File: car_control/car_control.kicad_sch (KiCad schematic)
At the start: 21 parts, among them J1 Conn_01x02, J2 Conn_01x03, J3 Conn_01x03, Q1 IRF540N, Q2 Q_Photo_NPN, SW1 SW_SPST

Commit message: initial schematic done?
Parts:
- added H1, H2, H3, H4: MountingHole, MountingHole:MountingHole_2.7mm_M2.5_DIN965_Pad, symbol Mechanical:MountingHole
- SW1: footprint Connector_PinHeader_2.54mm:PinHeader_1x02_P2.54mm_Vertical -> mini_slide_switch:OS102011MA1QN1; CatNo (none) -> CKN9559-ND
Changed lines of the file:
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@@
+    )
+  )
+  (symbol (lib_id "Mechanical:MountingHole") (at 44.45 129.54 0) (unit 1)
+    (in_bom yes) (on_board yes) (dnp no) (fields_autoplaced)
+    (property "Reference" "H1" (at 46.99 128.905 0)
+      (effects (font (size 1.27 1.27)) (justify left))
+    )
+    (property "Value" "MountingHole" (at 46.99 131.445 0)
+      (effects (font (size 1.27 1.27)) (justify left))
+    )
+    (property "Footprint" "MountingHole:MountingHole_2.7mm_M2.5_DIN965_Pad" (at 44.45 129.54 0)
+      (effects (font (size 1.27 1.27)) hide)
+    )
+    (property "Datasheet" "~" (at 44.45 129.54 0)
+      (effects (font (size 1.27 1.27)) hide)
+    )
+    (instances
+      (project "car_control"
+        (path "/08ff0388-b5fa-44e5-b165-5596a9674913"
+          (reference "H1") (unit 1)
+        )
+      )
     )
   )
@@
     )
   )
+  (symbol (lib_id "Mechanical:MountingHole") (at 44.45 148.59 0) (unit 1)
+    (in_bom yes) (on_board yes) (dnp no) (fields_autoplaced)
+    (property "Reference" "H4" (at 46.99 147.955 0)
+      (effects (font (size 1.27 1.27)) (justify left))
+    )
+    (property "Value" "MountingHole" (at 46.99 150.495 0)
+      (effects (font (size 1.27 1.27)) (justify left))
+    )
+    (property "Footprint" "MountingHole:MountingHole_2.7mm_M2.5_DIN965_Pad" (at 44.45 148.59 0)
+      (effects (font (size 1.27 1.27)) hide)
+    )
+    (property "Datasheet" "~" (at 44.45 148.59 0)
+      (effects (font (size 1.27 1.27)) hide)
+    )
+    (instances
+      (project "car_control"
+        (path "/08ff0388-b5fa-44e5-b165-5596a9674913"
+          (reference "H4") (unit 1)
+        )
+      )
+    )
+  )
   (symbol (lib_id "Device:LED") (at 144.78 113.03 180) (unit 1)
     (in_bom yes) (on_board yes) (dnp no)
@@
         (path "/08ff0388-b5fa-44e5-b165-5596a9674913"
           (reference "BT1") (unit 1)
+        )
+      )
+    )
+  )
+  (symbol (lib_id "Mechanical:MountingHole") (at 44.45 135.89 0) (unit 1)
+    (in_bom yes) (on_board yes) (dnp no) (fields_autoplaced)
+    (property "Reference" "H2" (at 46.99 135.255 0)
+      (effects (font (size 1.27 1.27)) (justify left))
+    )
+    (property "Value" "MountingHole" (at 46.99 137.795 0)
+      (effects (font (size 1.27 1.27)) (justify left))
+    )
+    (property "Footprint" "MountingHole:MountingHole_2.7mm_M2.5_DIN965_Pad" (at 44.45 135.89 0)
+      (effects (font (size 1.27 1.27)) hide)
+    )
+    (property "Datasheet" "~" (at 44.45 135.89 0)
+      (effects (font (size 1.27 1.27)) hide)
+    )
+    (instances
+      (project "car_control"
+        (path "/08ff0388-b5fa-44e5-b165-5596a9674913"
+          (reference "H2") (unit 1)
+        )
+      )
+    )
+  )
+  (symbol (lib_id "Mechanical:MountingHole") (at 44.45 142.24 0) (unit 1)
+    (in_bom yes) (on_board yes) (dnp no) (fields_autoplaced)
+    (property "Reference" "H3" (at 46.99 141.605 0)
+      (effects (font (size 1.27 1.27)) (justify left))
+    )
+    (property "Value" "MountingHole" (at 46.99 144.145 0)
+      (effects (font (size 1.27 1.27)) (justify left))
+    )
+    (property "Footprint" "MountingHole:MountingHole_2.7mm_M2.5_DIN965_Pad" (at 44.45 142.24 0)
+      (effects (font (size 1.27 1.27)) hide)
+    )
+    (property "Datasheet" "~" (at 44.45 142.24 0)
+      (effects (font (size 1.27 1.27)) hide)
+    )
+    (instances
+      (project "car_control"
+        (path "/08ff0388-b5fa-44e5-b165-5596a9674913"
+          (reference "H3") (unit 1)
         )
       )
@@
   )
   (symbol (lib_id "Switch:SW_SPST") (at 58.42 46.99 0) (unit 1)
-    (in_bom yes) (on_board yes) (dnp no) (fields_autoplaced)
-    (property "Reference" "SW1" (at 58.42 41.91 0)
-      (effects (font (size 1.27 1.27)))
-    )
-    (property "Value" "SW_SPST" (at 58.42 44.45 0)
-      (effects (font (size 1.27 1.27)))
-    )
-    (property "Footprint" "Connector_PinHeader_2.54mm:PinHeader_1x02_P2.54mm_Vertical" (at 58.42 46.99 0)
+    (in_bom yes) (on_board yes) (dnp no)
+    (property "Reference" "SW1" (at 50.8 43.18 0)
+      (effects (font (size 1.27 1.27)))
+    )
+    (property "Value" "SW_SPST" (at 64.77 43.18 0)
+      (effects (font (size 1.27 1.27)))
+    )
+    (property "Footprint" "mini_slide_switch:OS102011MA1QN1" (at 58.42 46.99 0)
       (effects (font (size 1.27 1.27)) hide)
     )
@@
       (effects (font (size 1.27 1.27)) hide)
     )
-    (pin "1")
+    (property "CatNo" "CKN9559-ND" (at 58.42 40.64 0)
+      (effects (font (size 1.27 1.27)))
+    )
+    (pin "1")

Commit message: working on mechanics
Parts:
- removed BT1: Battery, Connector_PinHeader_2.54mm:PinHeader_1x02_P2.54mm_Vertical, symbol Device:Battery
- removed J1: Conn_01x02, Connector_PinHeader_2.54mm:PinHeader_1x02_P2.54mm_Vertical, symbol Connector_Generic:Conn_01x02
- added J1, J4: Screw_Terminal_01x02, Connector_Wuerth:Wuerth_WR-WTB_64800211622_1x02_P1.50mm_Vertical, symbol Connector:Screw_Terminal_01x02
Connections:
- net GND: now also J4.2 (Pin_2)
- net at D1.2 (A), SW1.2 (B): now also J1.1 (Pin_1)
- net at D2.1 (K), Q1.2 (D): now also J1.2 (Pin_2)
- net at SW1.1 (A): now also J4.1 (Pin_1)
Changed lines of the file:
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@@
     (stroke (width 0) (type default))
   )
-  (wire (pts (xy 48.26 58.42) (xy 48.26 59.69))
+  (wire (pts (xy 48.26 54.61) (xy 48.26 59.69))
     (stroke (width 0) (type default))
   )
@@
     (stroke (width 0) (type default))
   )
-  (wire (pts (xy 48.26 46.99) (xy 48.26 48.26))
+  (wire (pts (xy 48.26 46.99) (xy 48.26 52.07))
     (stroke (width 0) (type default))
   )
@@
     (stroke (width 0) (type default))
   )
-  (text "6V battery pack\n(4x AA)" (at 27.94 55.88 0)
+  (text "6V battery pack\n(4x AA)" (at 21.59 49.53 0)
     (effects (font (size 1.27 1.27)) (justify left bottom))
   )
@@
     )
   )
-  (symbol (lib_id "Connector_Generic:Conn_01x02") (at 161.29 53.34 0) (unit 1)
+  (symbol (lib_id "Connector:Screw_Terminal_01x02") (at 161.29 53.34 0) (unit 1)
     (in_bom yes) (on_board yes) (dnp no) (fields_autoplaced)
     (property "Reference" "J1" (at 163.83 53.975 0)
       (effects (font (size 1.27 1.27)) (justify left))
     )
-    (property "Value" "Conn_01x02" (at 163.83 56.515 0)
-      (effects (font (size 1.27 1.27)) (justify left))
-    )
-    (property "Footprint" "Connector_PinHeader_2.54mm:PinHeader_1x02_P2.54mm_Vertical" (at 161.29 53.34 0)
+    (property "Value" "Screw_Terminal_01x02" (at 163.83 56.515 0)
+      (effects (font (size 1.27 1.27)) (justify left))
+    )
+    (property "Footprint" "Connector_Wuerth:Wuerth_WR-WTB_64800211622_1x02_P1.50mm_Vertical" (at 161.29 53.34 0)
       (effects (font (size 1.27 1.27)) hide)
     )
     (property "Datasheet" "~" (at 161.29 53.34 0)
+      (effects (font (size 1.27 1.27)) hide)
+    )
+    (property "CatNo" "A122765-ND" (at 161.29 53.34 0)
       (effects (font (size 1.27 1.27)) hide)
     )
@@
     )
   )
-  (symbol (lib_id "Device:Battery") (at 48.26 53.34 0) (unit 1)
-    (in_bom yes) (on_board yes) (dnp no) (fields_autoplaced)
-    (property "Reference" "BT1" (at 52.07 52.324 0)
-      (effects (font (size 1.27 1.27)) (justify left))
-    )
-    (property "Value" "Battery" (at 52.07 54.864 0)
-      (effects (font (size 1.27 1.27)) (justify left))
-    )
-    (property "Footprint" "Connector_PinHeader_2.54mm:PinHeader_1x02_P2.54mm_Vertical" (at 48.26 51.816 90)
-      (effects (font (size 1.27 1.27)) hide)
-    )
-    (property "Datasheet" "~" (at 48.26 51.816 90)
-      (effects (font (size 1.27 1.27)) hide)
-    )
-    (pin "1")
-    (pin "2")
-    (instances
-      (project "car_control"
-        (path "/08ff0388-b5fa-44e5-b165-5596a9674913"
-          (reference "BT1") (unit 1)
-        )
-      )
+  (symbol (lib_id "Connector:Screw_Terminal_01x02") (at 43.18 52.07 0) (mirror y) (unit 1)
+    (in_bom yes) (on_board yes) (dnp no)
+    (property "Reference" "J4" (at 40.64 52.705 0)
+      (effects (font (size 1.27 1.27)) (justify left))
+    )
+    (property "Value" "Screw_Terminal_01x02" (at 40.64 55.245 0)
+      (effects (font (size 1.27 1.27)) (justify left))
+    )
+    (property "Footprint" "Connector_Wuerth:Wuerth_WR-WTB_64800211622_1x02_P1.50mm_Vertical" (at 43.18 52.07 0)
+      (effects (font (size 1.27 1.27)) hide)
+    )
+    (property "Datasheet" "~" (at 43.18 52.07 0)
+      (effects (font (size 1.27 1.27)) hide)
+    )
+    (property "CatNo" "A122765-ND" (at 38.1 58.42 0)
+      (effects (font (size 1.27 1.27)))
+    )
+    (pin "1")
+    (pin "2")
+    (instances
+      (project "car_control"
+        (path "/08ff0388-b5fa-44e5-b165-5596a9674913"
+          (reference "J4") (unit 1)
+        )
+      )

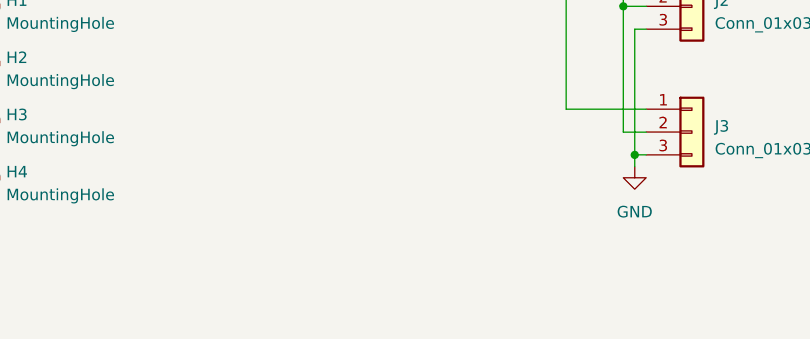
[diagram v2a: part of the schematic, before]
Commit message: New board outline with wings
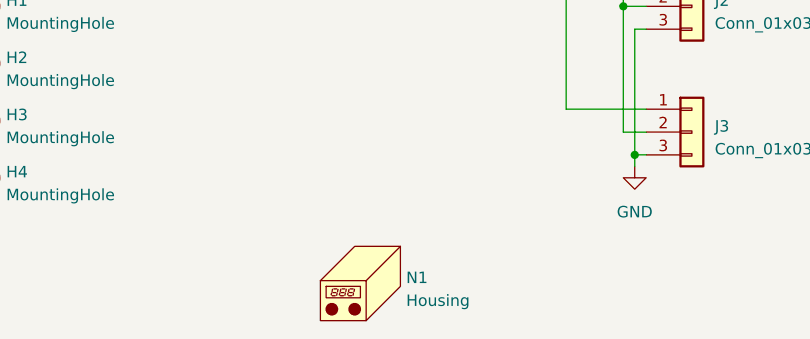
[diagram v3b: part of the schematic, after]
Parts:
- added N1: Housing, rhett_logo:rhett_logo, symbol Mechanical:Housing
- D4, D5, D6, D7: footprint LED_THT:LED_D3.0mm_Clear -> LED_THT:LED_D3.0mm_Horizontal_O3.81mm_Z2.0mm
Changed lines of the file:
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@@
       (effects (font (size 1.27 1.27)))
     )
-    (property "Footprint" "LED_THT:LED_D3.0mm_Clear" (at 144.78 97.79 0)
+    (property "Footprint" "LED_THT:LED_D3.0mm_Horizontal_O3.81mm_Z2.0mm" (at 144.78 97.79 0)
       (effects (font (size 1.27 1.27)) hide)
     )
@@
         (path "/08ff0388-b5fa-44e5-b165-5596a9674913"
           (reference "D4") (unit 1)
+        )
+      )
+    )
+  )
+  (symbol (lib_id "Mechanical:Housing") (at 87.63 160.02 0) (unit 1)
+    (in_bom yes) (on_board yes) (dnp no) (fields_autoplaced)
+    (property "Reference" "N1" (at 91.44 159.7025 0)
+      (effects (font (size 1.27 1.27)) (justify left))
+    )
+    (property "Value" "Housing" (at 91.44 162.2425 0)
+      (effects (font (size 1.27 1.27)) (justify left))
+    )
+    (property "Footprint" "rhett_logo:rhett_logo" (at 88.9 158.75 0)
+      (effects (font (size 1.27 1.27)) hide)
+    )
+    (property "Datasheet" "~" (at 88.9 158.75 0)
+      (effects (font (size 1.27 1.27)) hide)
+    )
+    (instances
+      (project "car_control"
+        (path "/08ff0388-b5fa-44e5-b165-5596a9674913"
+          (reference "N1") (unit 1)
         )
       )
@@
       (effects (font (size 1.27 1.27)))
     )
-    (property "Footprint" "LED_THT:LED_D3.0mm_Clear" (at 144.78 105.41 0)
+    (property "Footprint" "LED_THT:LED_D3.0mm_Horizontal_O3.81mm_Z2.0mm" (at 144.78 105.41 0)
       (effects (font (size 1.27 1.27)) hide)
     )
@@
       (effects (font (size 1.27 1.27)))
     )
-    (property "Footprint" "LED_THT:LED_D3.0mm_Clear" (at 144.78 113.03 0)
+    (property "Footprint" "LED_THT:LED_D3.0mm_Horizontal_O3.81mm_Z2.0mm" (at 144.78 113.03 0)
       (effects (font (size 1.27 1.27)) hide)
     )
@@
       (effects (font (size 1.27 1.27)))
     )
-    (property "Footprint" "LED_THT:LED_D3.0mm_Clear" (at 144.78 120.65 0)
-      (effects (font (size 1.27 1.27)) hide)
-    )
+    (property "Footprint" "LED_THT:LED_D3.0mm_Horizontal_O3.81mm_Z2.0mm" (at 144.78 120.65 0)
+      (effects (font (size 1.27 1.27)) hide)
+    )

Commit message: candidate placement
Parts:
- removed D3: IR_LED, LED_THT:LED_D3.0mm_Clear, symbol Device:LED
- removed Q2: Q_Photo_NPN, LED_THT:LED_D3.0mm_Clear, symbol Device:Q_Photo_NPN
- added U1: TCRT5000, my_opto:TCRT5000, symbol my_opto:Opto_Prox
- J1, J4: footprint Connector_Wuerth:Wuerth_WR-WTB_64800211622_1x02_P1.50mm_Vertical -> my_terminal:Wuerth_WR-WTB_64800211622_1x02_P1.50mm_Vertical
- Q1: footprint Package_TO_SOT_THT:TO-220-3_Vertical -> Package_TO_SOT_THT:TO-220-3_Horizontal_TabDown
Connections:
- net A0: now also U1.3 (C)
- net GND: now also U1.2 (C), U1.4 (E)
- net at R1.2: now also U1.1 (A)
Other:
- note added: "Headlights and tail lights"
- note added: "Optical proximity sensor"
- note removed: "LEDs for fun!"
- note removed: "Optical distance sensor"
- moved on the sheet: R2

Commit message: routing
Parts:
- removed H4: MountingHole, MountingHole:MountingHole_2.7mm_M2.5_DIN965_Pad, symbol Mechanical:MountingHole
- added D3: 1N4004, Diode_THT:D_DO-41_SOD81_P10.16mm_Horizontal, symbol Diode:1N4004
- added LS1: Speaker, my_terminal:speaker_d12mm_h8.5_p6.5, symbol Device:Speaker
- added Q2: 2N3904, Package_TO_SOT_THT:TO-92_Inline, symbol Transistor_BJT:2N3904
- added R7: 470, Resistor_THT:R_Axial_DIN0207_L6.3mm_D2.5mm_P10.16mm_Horizontal, symbol Device:R_US
- added SW2: SW_Push, my_pushbutton:sw_push_6.2x6.2mm_p5, symbol Switch:SW_Push
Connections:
- net +5V: now also D3.1 (K), LS1.1
- net GND: now also Q2.1 (E), SW2.1
- net at A1.14 (D16): now also R7.2
- net at A1.18 (A1): now also SW2.2
- new net: Q2.2 (B), R7.1
- new net: D3.2 (A), LS1.2, Q2.3 (C)
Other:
- moved on the sheet: N1

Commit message: first version done?
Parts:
- added N2: Housing, car_as:car_as, symbol Mechanical:Housing
- A1: footprint Package_DIP:DIP-24_W15.24mm_Socket -> my_arduino:pro_micro_socket
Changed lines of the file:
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@@
+    )
+  )
+  (symbol (lib_id "Mechanical:Housing") (at 46.99 175.26 0) (unit 1)
+    (in_bom yes) (on_board yes) (dnp no) (fields_autoplaced)
+    (property "Reference" "N2" (at 50.8 174.9425 0)
+      (effects (font (size 1.27 1.27)) (justify left))
+    )
+    (property "Value" "Housing" (at 50.8 177.4825 0)
+      (effects (font (size 1.27 1.27)) (justify left))
+    )
+    (property "Footprint" "car_as:car_as" (at 48.26 173.99 0)
+      (effects (font (size 1.27 1.27)) hide)
+    )
+    (property "Datasheet" "~" (at 48.26 173.99 0)
+      (effects (font (size 1.27 1.27)) hide)
+    )
+    (instances
+      (project "car_control"
+        (path "/08ff0388-b5fa-44e5-b165-5596a9674913"
+          (reference "N2") (unit 1)
+        )
+      )
     )
   )
@@
       (effects (font (size 1.27 1.27)) (justify left))
     )
-    (property "Footprint" "Package_DIP:DIP-24_W15.24mm_Socket" (at 88.9 90.17 0)
+    (property "Footprint" "my_arduino:pro_micro_socket" (at 88.9 90.17 0)
       (effects (font (size 1.27 1.27) italic) hide)
     )
